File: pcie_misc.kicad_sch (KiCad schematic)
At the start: 38 parts, among them U37 9DBL0651CKILF, U38 74AUP2G132, Y1 Oscillator_32.768kHz_ECS_2520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

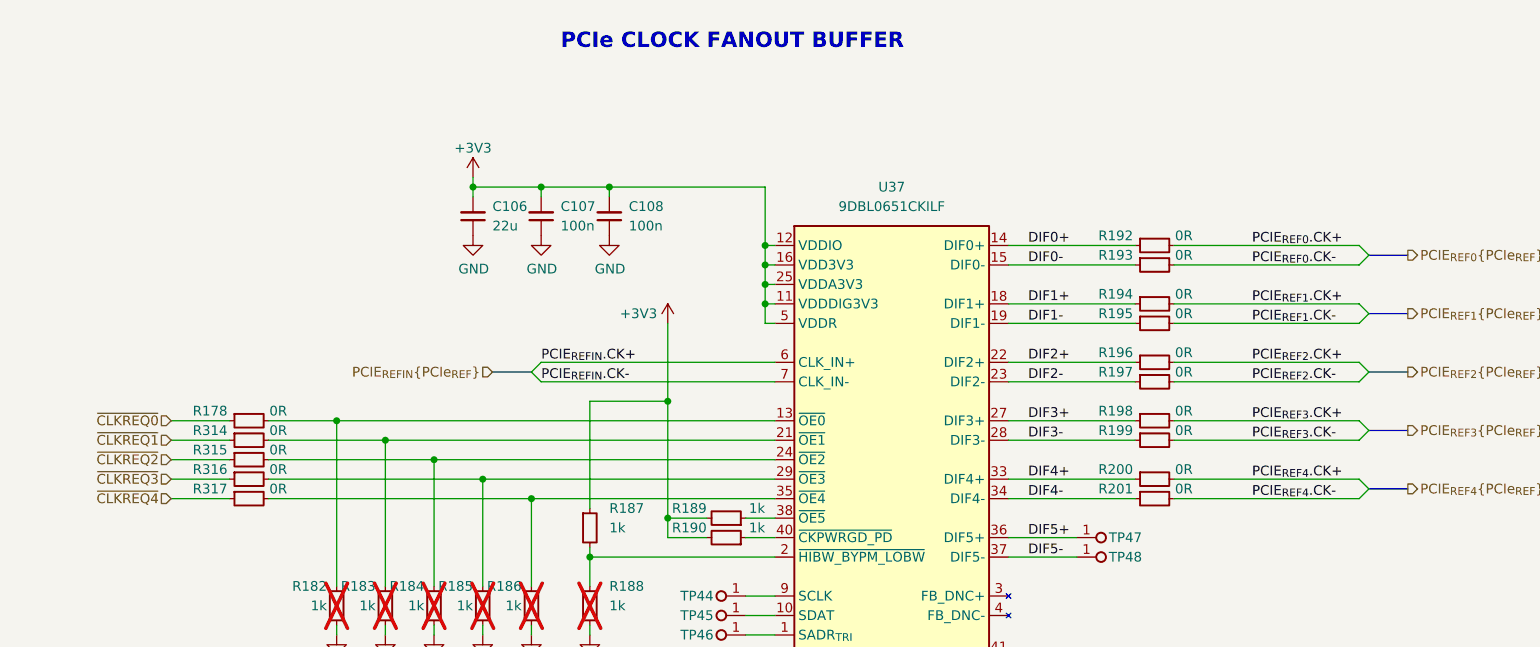
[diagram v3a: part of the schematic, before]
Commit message: [#65840] Route PCIe clock fanout, improve PCIe lines layout
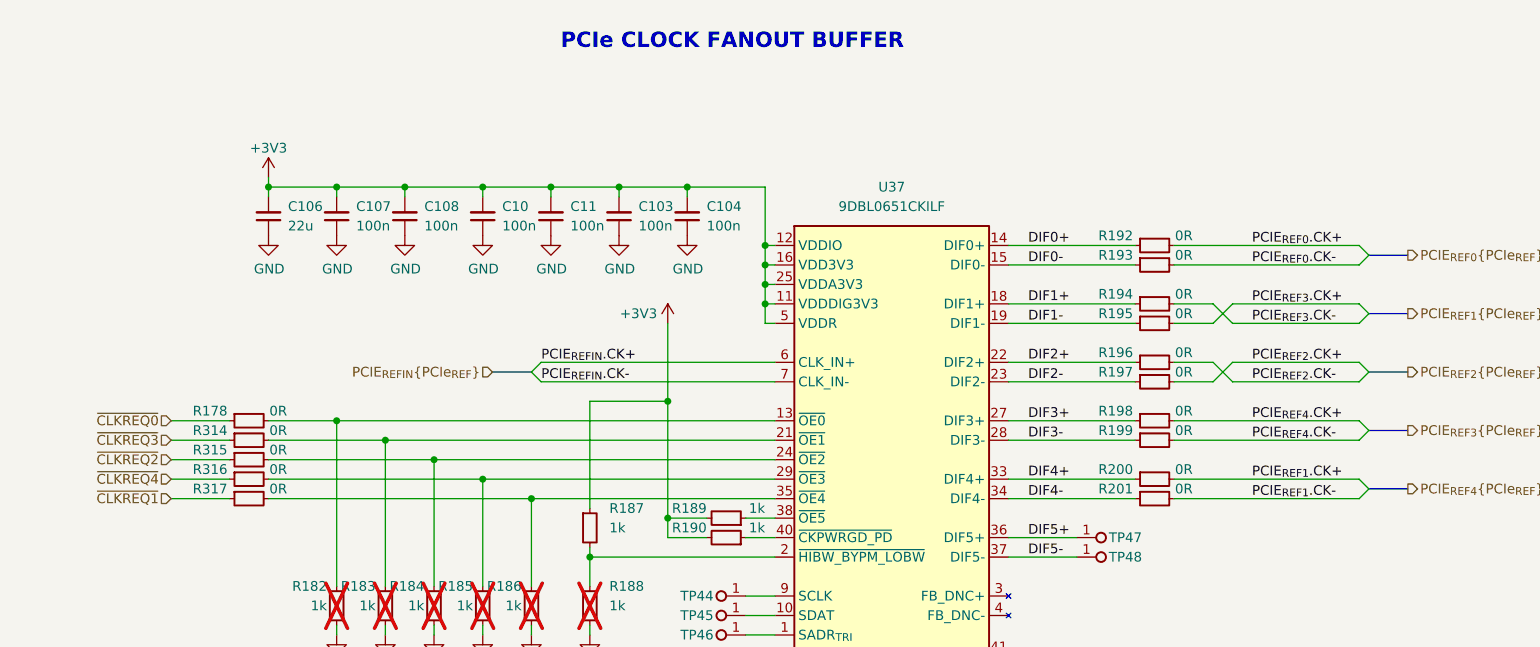
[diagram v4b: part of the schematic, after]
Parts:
- added C10, C103, C104, C11: C_100n_0402, antmicro-footprints:C_0402_1005Metric, symbol antmicroCapacitors0402:C_100n_0402
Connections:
- net +3V3: now also C10.2, C103.2, C104.2, C11.2
- net GND: now also C10.1, C103.1, C104.1, C11.1
- net PCIE_{REF1}.CK+: now also R200.2; no longer R194.2
- net PCIE_{REF1}.CK-: now also R201.2; no longer R195.2
- net PCIE_{REF2}.CK+: now also R197.2; no longer R196.2
- net PCIE_{REF2}.CK-: now also R196.2; no longer R197.2
- net PCIE_{REF3}.CK+: now also R195.2; no longer R198.2
- net PCIE_{REF3}.CK-: now also R194.2; no longer R199.2
- net PCIE_{REF4}.CK+: now also R198.2; no longer R200.2
- net PCIE_{REF4}.CK-: now also R199.2; no longer R201.2
- net ~{CLKREQ1}: now also R317.1; no longer R314.1
- net ~{CLKREQ3}: now also R314.1; no longer R316.1
- net ~{CLKREQ4}: now also R316.1; no longer R317.1
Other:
- moved on the sheet: C106, C107, C108

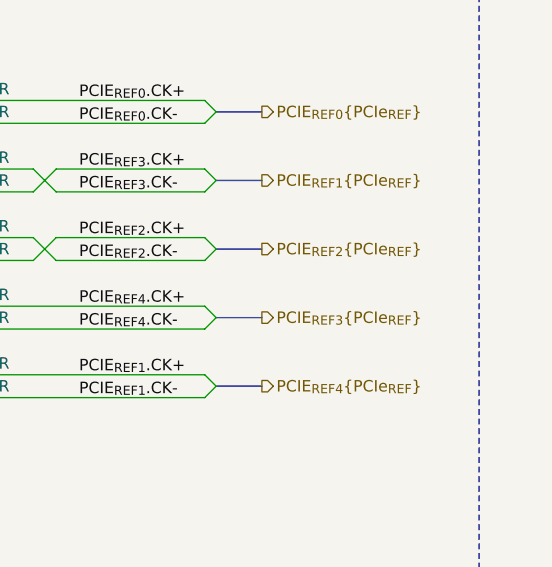
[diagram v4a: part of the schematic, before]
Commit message: [#66613] Fix ERC, adjust overlapping text on schematic
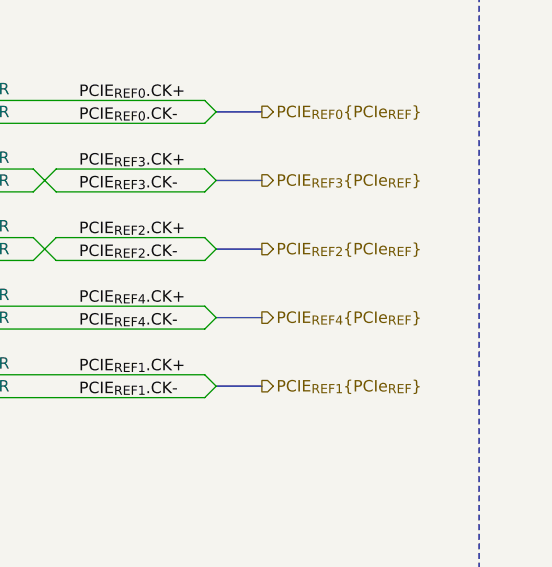
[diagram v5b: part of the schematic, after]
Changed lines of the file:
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@@
+    (stroke (width 0) (type default))
+  )
+  (wire (pts (xy 142.24 81.28) (xy 158.75 81.28))
+    (stroke (width 0) (type default))
+  )
+  (wire (pts (xy 91.44 50.8) (xy 91.44 52.07))
+    (stroke (width 0) (type default))
+  )
+  (wire (pts (xy 33.02 81.28) (xy 40.64 81.28))
     (stroke (width 0) (type default))
   )
@@
     (stroke (width 0) (type default))
   )
-  (wire (pts (xy 142.24 81.28) (xy 158.75 81.28))
-    (stroke (width 0) (type default))
-  )
-  (wire (pts (xy 91.44 50.8) (xy 91.44 52.07))
-    (stroke (width 0) (type default))
-  )
-  (wire (pts (xy 33.02 81.28) (xy 40.64 81.28))
-    (stroke (width 0) (type default))
-  )
   (wire (pts (xy 45.72 88.9) (xy 73.66 88.9))
     (stroke (width 0) (type default))
@@
   )
   (wire (pts (xy 91.44 210.82) (xy 91.44 212.09))
-    (stroke (width 0) (type default))
-  )
-  (bus (pts (xy 189.23 82.55) (xy 194.31 82.55))
     (stroke (width 0) (type default))
   )
@@
     (stroke (width 0) (type default))
   )
+  (bus (pts (xy 189.23 67.31) (xy 194.31 67.31))
+    (stroke (width 0) (type default))
+  )
   (wire (pts (xy 123.19 215.9) (xy 123.19 217.17))
     (stroke (width 0) (type default))
@@
     (stroke (width 0) (type default))
   )
-  (bus (pts (xy 189.23 67.31) (xy 194.31 67.31))
+  (bus (pts (xy 189.23 82.55) (xy 194.31 82.55))
     (stroke (width 0) (type default))
   )
@@
     (effects (font (size 1.27 1.27)) (justify left bottom))
   )
+  (hierarchical_label "PCIE_{REF4}{PCIe_{REF}}" (shape output) (at 194.31 82.55 0) (fields_autoplaced)
+    (effects (font (size 1.27 1.27)) (justify left))
+  )
+  (hierarchical_label "PCIE_{REF3}{PCIe_{REF}}" (shape output) (at 194.31 67.31 0) (fields_autoplaced)
+    (effects (font (size 1.27 1.27)) (justify left))
+  )
   (hierarchical_label "~{CLKREQ3}" (shape input) (at 33.02 83.82 180) (fields_autoplaced)
     (effects (font (size 1.27 1.27)) (justify right))
@@
     (effects (font (size 1.27 1.27)) (justify left))
   )
-  (hierarchical_label "PCIE_{REF4}{PCIe_{REF}}" (shape output) (at 194.31 90.17 0) (fields_autoplaced)
-    (effects (font (size 1.27 1.27)) (justify left))
-  )
   (hierarchical_label "~{CLKREQ4}" (shape input) (at 33.02 88.9 180) (fields_autoplaced)
     (effects (font (size 1.27 1.27)) (justify right))
@@
     (effects (font (size 1.27 1.27)) (justify right))
   )
-  (hierarchical_label "PCIE_{REF1}{PCIe_{REF}}" (shape output) (at 194.31 67.31 0) (fields_autoplaced)
-    (effects (font (size 1.27 1.27)) (justify left))
-  )
-  (hierarchical_label "PCIE_{REF3}{PCIe_{REF}}" (shape output) (at 194.31 82.55 0) (fields_autoplaced)
-    (effects (font (size 1.27 1.27)) (justify left))
-  )
   (hierarchical_label "~{CLKREQ1}" (shape input) (at 33.02 91.44 180) (fields_autoplaced)
     (effects (font (size 1.27 1.27)) (justify right))
@@
     (effects (font (size 1.27 1.27)) (justify right))
   )
+  (hierarchical_label "PCIE_{REF1}{PCIe_{REF}}" (shape output) (at 194.31 90.17 0) (fields_autoplaced)
+    (effects (font (size 1.27 1.27)) (justify left))
+  )
   (hierarchical_label "~{CLKREQ2}" (shape input) (at 33.02 86.36 180) (fields_autoplaced)
